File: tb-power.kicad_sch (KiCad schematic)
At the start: 62 parts, among them Q1 BC817-25W, U13 MCP6541_SOT23-5_Split, U4 JHL6340SLLSQ

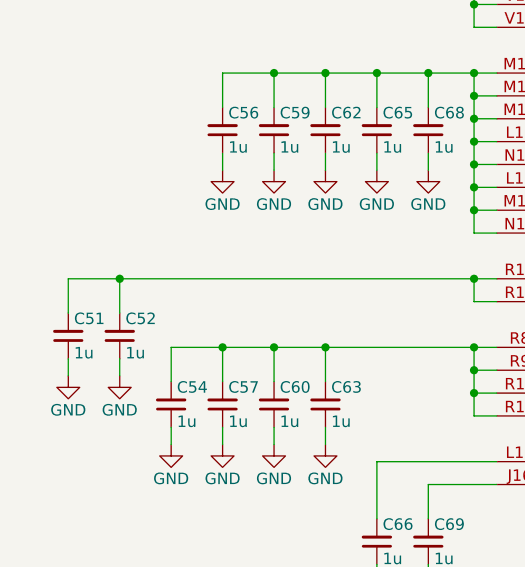
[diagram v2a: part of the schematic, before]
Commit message: Fix ERC errors on schematic:
	- Fix first batch of GND ERC
	- Fix second batch of GND ERC
	- Fix ERC of 0R_0603
	- Fix erc BC817-25W
	- Fix erc 220n_0402
	- Fix erc PCIe_x16_10146070-113Y0LF-vertical
	- Fix erc 100n_0402
	- Fix erc 10u_0805_35V
	- Correct BC817-25W_1
	- Correct erc R_98R_0402_1
	- Correct 10K_0402
	- Correct 22u/16V
	- Correct 100k
	- Correct 499R
	- Correct 3k01
	- Correct 10p
	- Correct 330R
	- Correct 3k3
	- Correct 1n4148WS-7-F
	- Correct SI7613DN-T1GE3_1 and TP's
	- Correct LED_G_0603_KP-1608CGCK_1
	- Correct 2k2_0402
	- Correct DZDH0401DW_1
	- Correct 22u_0603
	- Correct TP 0.75mm
	- Correct 0R_0402
	- Correct 0R_22.4A
	- Correct Batch of Resitors
	- Correct Batch of Capacitors
	- Correct USB PD controller
	- Correct batch of pasives
	- Correct MM3Z3V3C
	- Correct LM1117MP-3.3_NOPB
	- Correct Flash memory
	- Correct MP2386GG_1_1
	- Fix symbol LT8350RV#PBF and correct it on schematic
	- Add pwr flags
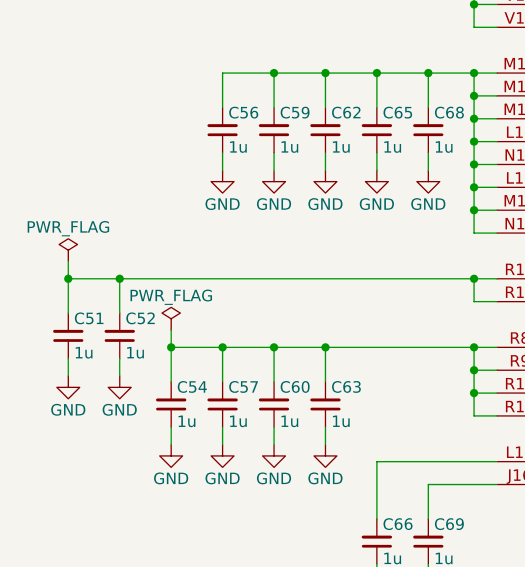
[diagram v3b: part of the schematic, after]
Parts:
- C70, C75, C76, C78, C80, C83, C96: Manufacturer Yaego -> YAGEO
- L4: IMax 1.8 -> 1.8A; ISat 1.9 -> 1.9A
- TP9: footprint thunderbolt-gpu-adapter-footprints:Testpoint_smd_1mm -> thunderbolt-gpu-adapter-footprints:TP_SMD_1mm

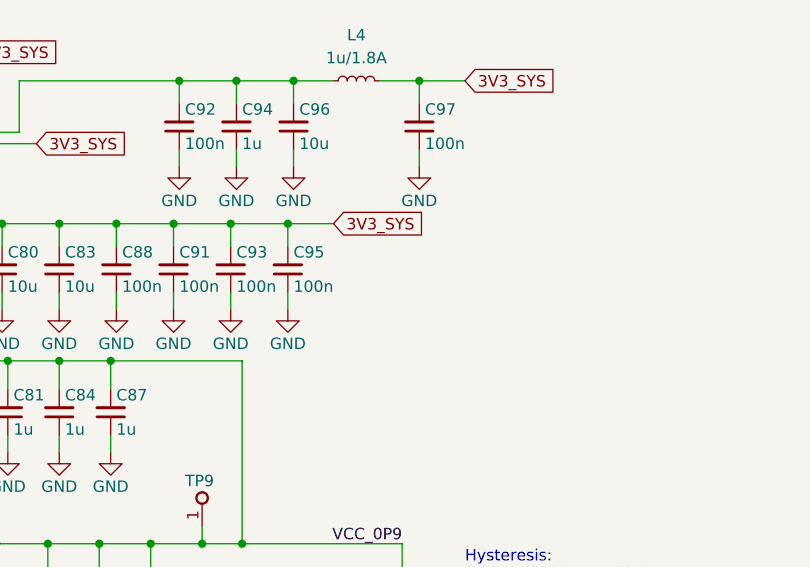
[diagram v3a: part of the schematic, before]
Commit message: Improved power filtration for TB controller
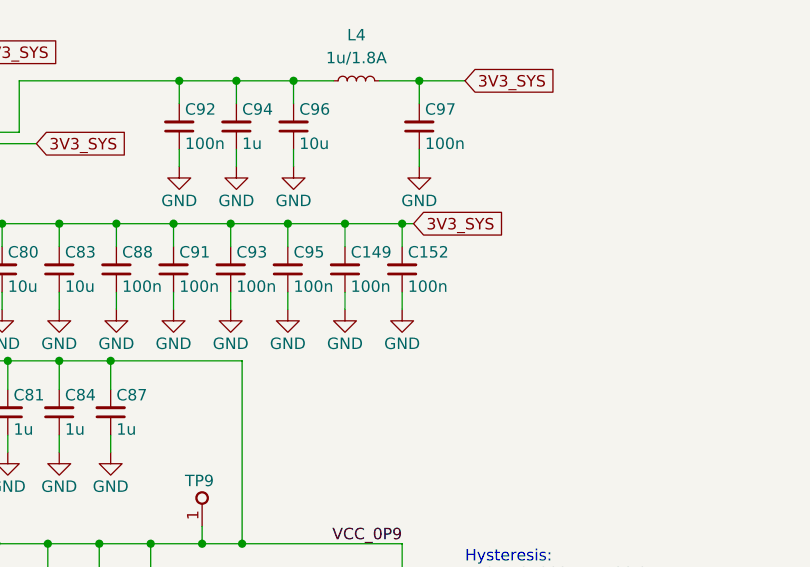
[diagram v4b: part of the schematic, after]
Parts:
- added C149, C152: C_100n_0402, thunderbolt-gpu-adapter-footprints:C_0402_1005Metric, symbol thunderbolt-gpu-adapter:C_100n_0402
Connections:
- net 3V3_SYS: now also C149.2, C152.2
- net GND: now also C149.1, C152.1
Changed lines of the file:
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@@
   (junction (at 116.84 245.11) (diameter 0) (color 0 0 0 0)
   )
+  (junction (at 229.87 90.17) (diameter 0) (color 0 0 0 0)
+  )
   (junction (at 175.26 229.87) (diameter 0) (color 0 0 0 0)
   )
@@
   (junction (at 175.26 311.15) (diameter 0) (color 0 0 0 0)
   )
+  (junction (at 236.22 90.17) (diameter 0) (color 0 0 0 0)
+  )
   (junction (at 116.84 308.61) (diameter 0) (color 0 0 0 0)
   )
@@
     (stroke (width 0) (type default) (color 0 0 0 0))
   )
+  (wire (pts (xy 236.22 90.17) (xy 237.49 90.17))
+    (stroke (width 0) (type default) (color 0 0 0 0))
+  )
   (wire (pts (xy 71.12 123.19) (xy 76.835 123.19))
     (stroke (width 0) (type default) (color 0 0 0 0))
@@
     (stroke (width 0) (type default) (color 0 0 0 0))
   )
-  (wire (pts (xy 223.52 90.17) (xy 228.6 90.17))
+  (wire (pts (xy 223.52 90.17) (xy 229.87 90.17))
     (stroke (width 0) (type default) (color 0 0 0 0))
   )
@@
     (stroke (width 0) (type default) (color 0 0 0 0))
   )
+  (wire (pts (xy 229.87 90.17) (xy 229.87 92.71))
+    (stroke (width 0) (type default) (color 0 0 0 0))
+  )
   (wire (pts (xy 243.84 166.37) (xy 243.84 163.83))
     (stroke (width 0) (type default) (color 0 0 0 0))
@@
     (stroke (width 0) (type default) (color 0 0 0 0))
   )
+  (wire (pts (xy 229.87 90.17) (xy 236.22 90.17))
+    (stroke (width 0) (type default) (color 0 0 0 0))
+  )
   (wire (pts (xy 116.84 186.69) (xy 118.745 186.69))
     (stroke (width 0) (type default) (color 0 0 0 0))
@@
     (stroke (width 0) (type default) (color 0 0 0 0))
   )
+  (wire (pts (xy 236.22 90.17) (xy 236.22 92.71))
+    (stroke (width 0) (type default) (color 0 0 0 0))
+  )
   (wire (pts (xy 203.835 113.665) (xy 203.835 115.57))
     (stroke (width 0) (type default) (color 0 0 0 0))
@@
     (stroke (width 0) (type default) (color 0 0 0 0))
   )
+  (wire (pts (xy 236.22 97.79) (xy 236.22 99.695))
+    (stroke (width 0) (type default) (color 0 0 0 0))
+  )
   (wire (pts (xy 118.745 123.19) (xy 116.205 123.19))
     (stroke (width 0) (type default) (color 0 0 0 0))
@@
     (stroke (width 0) (type default) (color 0 0 0 0))
   )
+  (wire (pts (xy 229.87 97.79) (xy 229.87 99.695))
+    (stroke (width 0) (type default) (color 0 0 0 0))
+  )
   (wire (pts (xy 88.265 69.85) (xy 88.265 73.66))
     (stroke (width 0) (type default) (color 0 0 0 0))
@@
     )
   )
-  (global_label "3V3_SYS" (shape input) (at 228.6 90.17 0) (fields_autoplaced)
+  (global_label "3V3_SYS" (shape input) (at 237.49 90.17 0) (fields_autoplaced)
     (effects (font (size 1.27 1.27)) (justify left))
-    (property "Intersheet References" "${INTERSHEET_REFS}" (id 0) (at 238.996 90.0906 0)
+    (property "Intersheet References" "${INTERSHEET_REFS}" (id 0) (at 247.886 90.0906 0)
       (effects (font (size 1.27 1.27)) (justify left) hide)
     )
@@
     (pin "2")
   )
+  (symbol (lib_id "thunderbolt-gpu-adapter:C_100n_0402") (at 229.87 97.79 90) (unit 1)
+    (in_bom yes) (on_board yes)
+    (property "Reference" "C149" (id 0) (at 230.505 93.345 90)
+      (effects (font (size 1.27 1.27) (thickness 0.15)) (justify right))
+    )
+    (property "Value" "C_100n_0402" (id 1) (at 240.03 77.47 0)
+      (effects (font (size 1.27 1.27) (thickness 0.15)) (justify left bottom) hide)
+    )
+    (property "Footprint" "thunderbolt-gpu-adapter-footprints:C_0402_1005Metric" (id 2) (at 242.57 77.47 0)
+      (effects (font (size 1.27 1.27) (thickness 0.15)) (justify left bottom) hide)
+    )
+    (property "Datasheet" "https://www.murata.com/products/productdetail?partno=GRM155R61H104KE14%23" (id 3) (at 245.11 77.47 0)
+      (effects (font (size 1.27 1.27) (thickness 0.15)) (justify left bottom) hide)
+    )
+    (property "MPN" "GRM155R61H104KE14D" (id 4) (at 247.65 77.47 0)
+      (effects (font (size 1.27 1.27) (thickness 0.15)) (justify left bottom) hide)
+    )
+    (property "Manufacturer" "Murata" (id 5) (at 250.19 77.47 0)
+      (effects (font (size 1.27 1.27) (thickness 0.15)) (justify left bottom) hide)
+    )
+    (property "License" "Apache-2.0" (id 6) (at 252.73 77.47 0)
+      (effects (font (size 1.27 1.27) (thickness 0.15)) (justify left bottom) hide)
+    )
+    (property "Val" "100n" (id 8) (at 230.505 97.155 90)
+      (effects (font (size 1.27 1.27) (thickness 0.15)) (justify right))
+    )
+    (property "Voltage" "50V" (id 9) (at 257.81 77.47 0)
+      (effects (font (size 1.27 1.27)) (justify left bottom) hide)
+    )
+    (property "Dielectric" "X5R" (id 10) (at 260.35 77.47 0)
+      (effects (font (size 1.27 1.27)) (justify left bottom) hide)
+    )
+    (property "Author" "Antmicro" (id 11) (at 255.27 77.47 0)
+      (effects (font (size 1.27 1.27) (thickness 0.15)) (justify left bottom) hide)
+    )
+    (pin "1")
+    (pin "2")
+  )
   (symbol (lib_name "C_1u_0402_11") (lib_id "thunderbolt-gpu-adapter:C_1u_0402") (at 71.12 132.08 90) (unit 1)
     (in_bom yes) (on_board yes)
@@
     (pin "2")
   )
+  (symbol (lib_id "thunderbolt-gpu-adapter:GND") (at 229.87 99.695 0) (unit 1)
+    (in_bom yes) (on_board yes)
+    (property "Reference" "#PWR0223" (id 0) (at 229.87 106.045 0)
+      (effects (font (size 1.27 1.27)) hide)
+    )
+    (property "Value" "GND" (id 1) (at 229.87 103.505 0))
+    (property "Footprint" "" (id 2) (at 229.87 99.695 0)
+      (effects (font (size 1.27 1.27)) hide)
+    )
+    (property "Datasheet" "" (id 3) (at 229.87 99.695 0)
+      (effects (font (size 1.27 1.27)) hide)
+    )
+    (property "Author" "Antmicro" (id 4) (at 238.76 107.315 0)
+      (effects (font (size 1.27 1.27) (thickness 0.15)) (justify left bottom) hide)
+    )
+    (property "License" "Apache-2.0" (id 5) (at 238.76 109.855 0)
+      (effects (font (size 1.27 1.27) (thickness 0.15)) (justify left bottom) hide)
+    )
+    (pin "1")
+  )
   (symbol (lib_id "thunderbolt-gpu-adapter:GND") (at 93.98 141.605 0) (unit 1)
     (in_bom yes) (on_board yes)
@@
     (pin "1")
   )
+  (symbol (lib_name "C_100n_0402_6") (lib_id "thunderbolt-gpu-adapter:C_100n_0402") (at 236.22 97.79 90) (unit 1)
+    (in_bom yes) (on_board yes)
+    (property "Reference" "C152" (id 0) (at 236.855 93.345 90)
+      (effects (font (size 1.27 1.27) (thickness 0.15)) (justify right))
+    )
+    (property "Value" "C_100n_0402" (id 1) (at 246.38 77.47 0)
+      (effects (font (size 1.27 1.27) (thickness 0.15)) (justify left bottom) hide)
+    )
+    (property "Footprint" "thunderbolt-gpu-adapter-footprints:C_0402_1005Metric" (id 2) (at 248.92 77.47 0)
+      (effects (font (size 1.27 1.27) (thickness 0.15)) (justify left bottom) hide)
+    )
+    (property "Datasheet" "https://www.murata.com/products/productdetail?partno=GRM155R61H104KE14%23" (id 3) (at 251.46 77.47 0)
+      (effects (font (size 1.27 1.27) (thickness 0.15)) (justify left bottom) hide)
+    )
+    (property "MPN" "GRM155R61H104KE14D" (id 4) (at 254 77.47 0)
+      (effects (font (size 1.27 1.27) (thickness 0.15)) (justify left bottom) hide)
+    )
+    (property "Manufacturer" "Murata" (id 5) (at 256.54 77.47 0)
+      (effects (font (size 1.27 1.27) (thickness 0.15)) (justify left bottom) hide)
+    )
+    (property "License" "Apache-2.0" (id 6) (at 259.08 77.47 0)
+      (effects (font (size 1.27 1.27) (thickness 0.15)) (justify left bottom) hide)
+    )
+    (property "Val" "100n" (id 8) (at 236.855 97.155 90)
+      (effects (font (size 1.27 1.27) (thickness 0.15)) (justify right))
+    )
+    (property "Voltage" "50V" (id 9) (at 264.16 77.47 0)
+      (effects (font (size 1.27 1.27)) (justify left bottom) hide)
+    )
+    (property "Dielectric" "X5R" (id 10) (at 266.7 77.47 0)
+      (effects (font (size 1.27 1.27)) (justify left bottom) hide)
+    )
+    (property "Author" "Antmicro" (id 11) (at 261.62 77.47 0)
+      (effects (font (size 1.27 1.27) (thickness 0.15)) (justify left bottom) hide)
+    )
+    (pin "1")
+    (pin "2")
+  )
   (symbol (lib_id "thunderbolt-gpu-adapter:GND") (at 184.15 74.93 90) (unit 1)
     (in_bom yes) (on_board yes)
@@
       (effects (font (size 1.27 1.27) (thickness 0.15)) (justify left bottom) hide)
     )
+    (pin "1")
+  )
+  (symbol (lib_id "thunderbolt-gpu-adapter:GND") (at 236.22 99.695 0) (unit 1)
+    (in_bom yes) (on_board yes)
+    (property "Reference" "#PWR0221" (id 0) (at 236.22 106.045 0)
+      (effects (font (size 1.27 1.27)) hide)
+    )
+    (property "Value" "GND" (id 1) (at 236.22 103.505 0))
+    (property "Footprint" "" (id 2) (at 236.22 99.695 0)
+      (effects (font (size 1.27 1.27)) hide)
+    )
+    (property "Datasheet" "" (id 3) (at 236.22 99.695 0)
+      (effects (font (size 1.27 1.27)) hide)
+    )
+    (property "Author" "Antmicro" (id 4) (at 245.11 107.315 0)
+      (effects (font (size 1.27 1.27) (thickness 0.15)) (justify left bottom) hide)
+    )
+    (property "License" "Apache-2.0" (id 5) (at 245.11 109.855 0)
+      (effects (font (size 1.27 1.27) (thickness 0.15)) (justify left bottom) hide)
+    )
